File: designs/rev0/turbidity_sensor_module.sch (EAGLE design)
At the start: 26 parts, among them IC1 LTC485S, IC2 TINY441

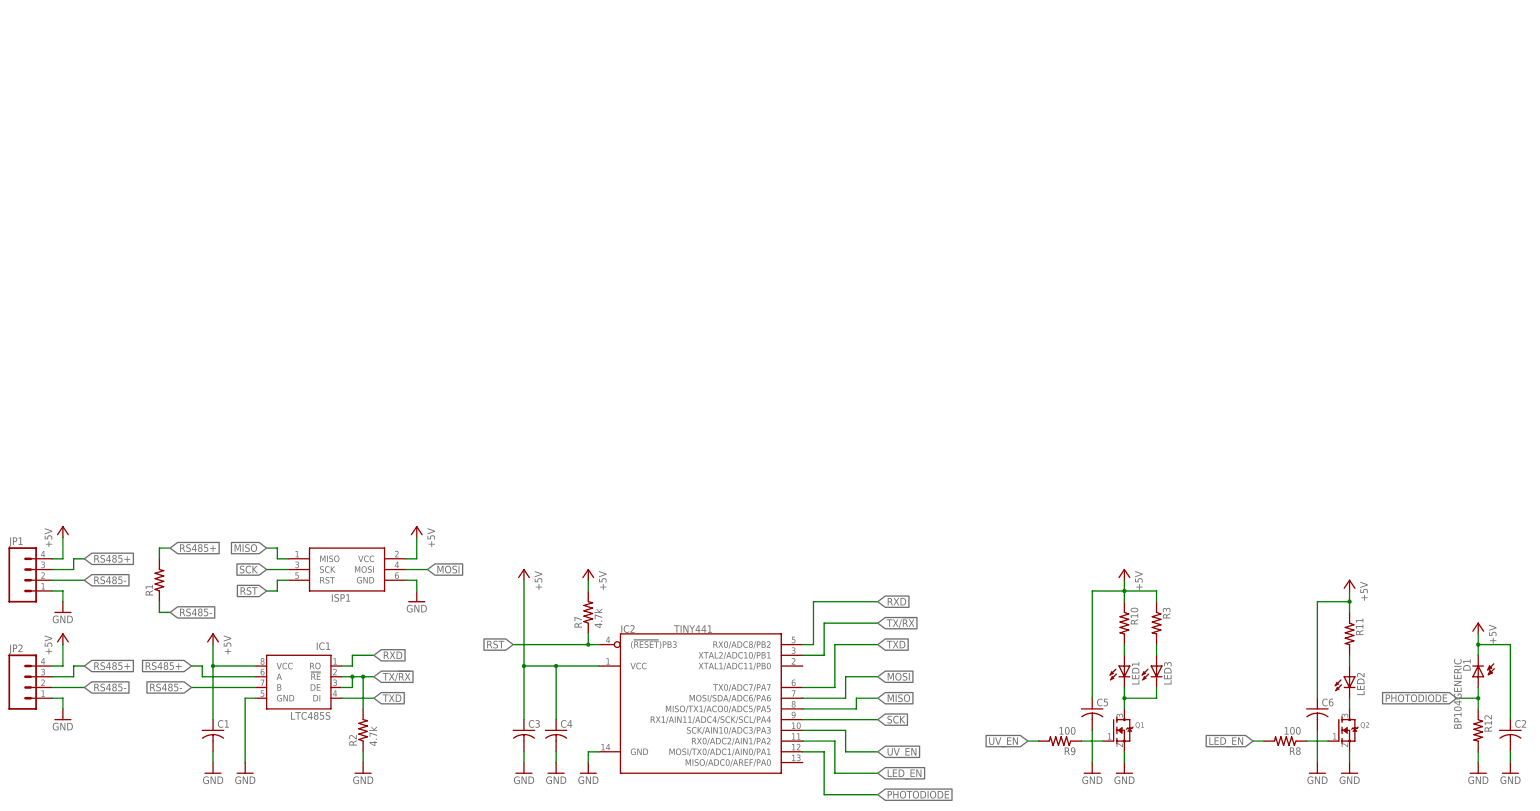
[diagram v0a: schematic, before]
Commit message: Put files into new folders
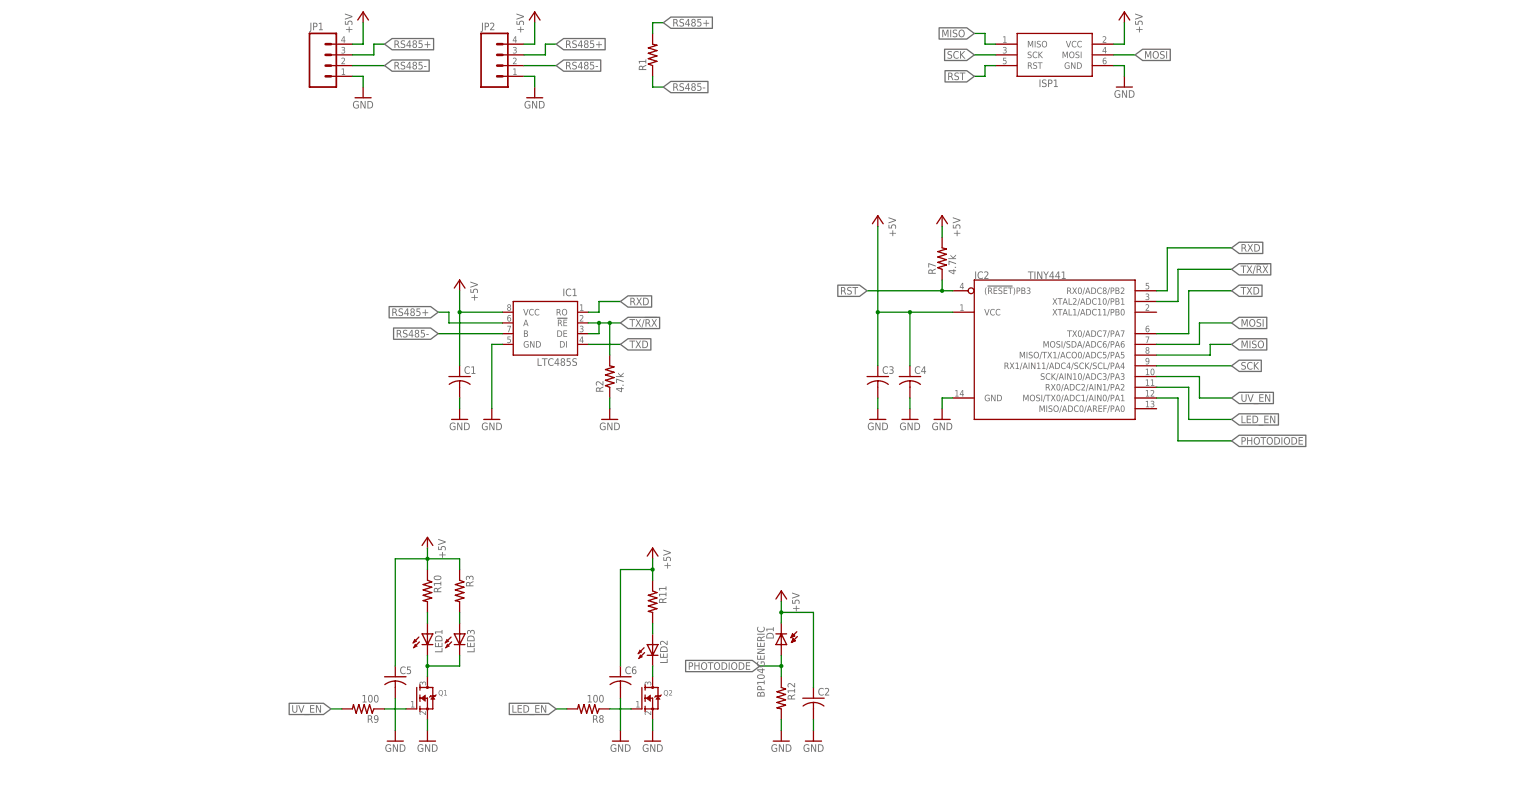
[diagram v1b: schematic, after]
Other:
- moved on the sheet: C1, C2, C3, C4, C5, C6, D1, IC1, IC2, ISP1, JP1, JP2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
